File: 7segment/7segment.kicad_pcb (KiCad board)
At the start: 4 copper layers, 22.5 x 25.1 mm, 31 parts, among them J1 AVR-ISP-6, J2 Conn_01x10, J3 Conn_01x02, J4 Conn_01x02, Q1 Q_NPN_BEC, Q2 Q_NPN_BEC, U1 ATmega168PA-AU, U2 HDSP-523

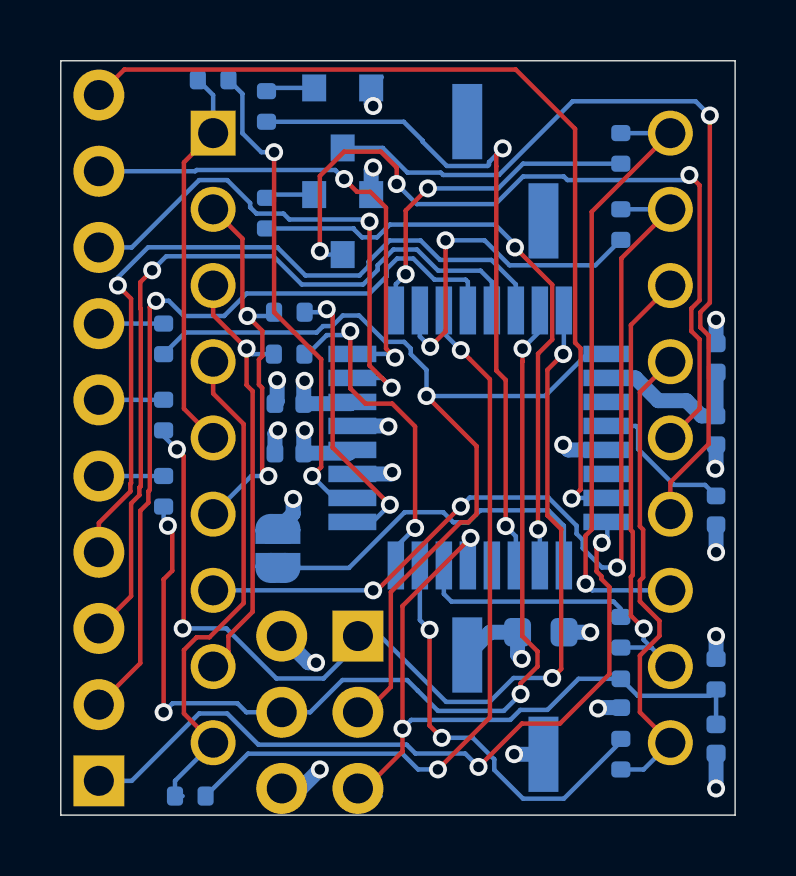
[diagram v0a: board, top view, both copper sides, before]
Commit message: Update 7segment
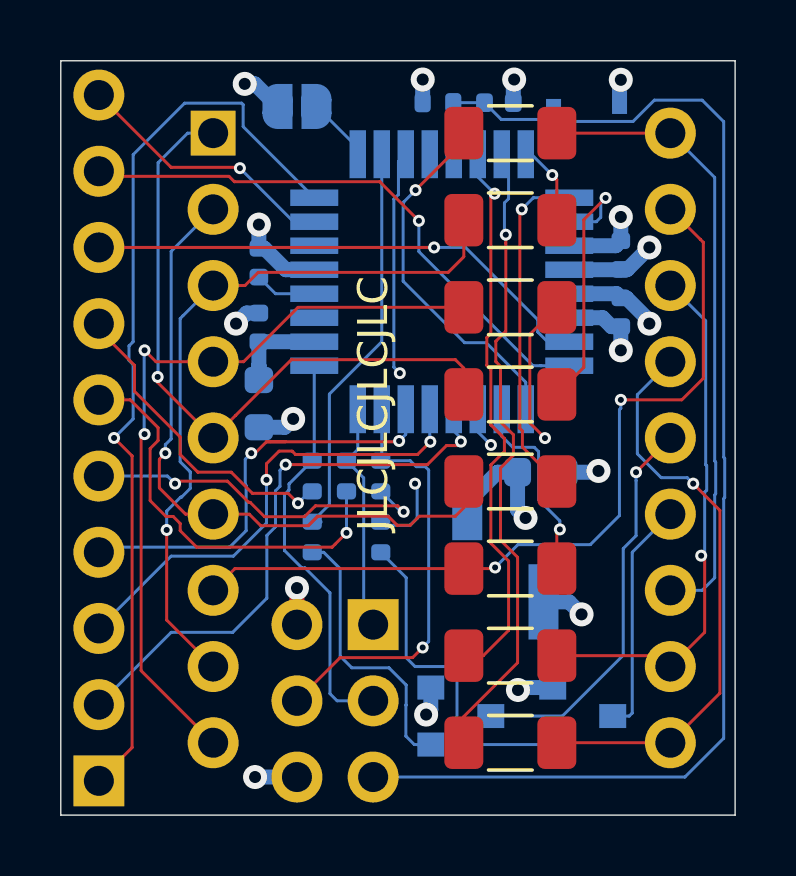
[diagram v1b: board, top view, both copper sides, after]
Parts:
- removed J3: Conn_01x02, Connector_PinHeader_2.54mm:PinHeader_1x02_P2.54mm_Vertical_SMD_Pin1Left
- D1: value D_TVS -> 1N4148; footprint Diode_SMD:D_0402_1005Metric -> Diode_SMD:D_SOD-323F
- L1: footprint Inductor_SMD:L_0402_1005Metric -> Inductor_SMD:L_0603_1608Metric
- R1, R2, R3, R4, R5, R6, R7, R8: footprint Resistor_SMD:R_0402_1005Metric -> Resistor_SMD:R_1206_3216Metric_Pad1.30x1.75mm_HandSolder; moved to F.Cu
- moved D1 21.5 mm to (138.2, 104.5), turned to 180 degrees
- moved Q2 21.5 mm to (138.0, 124.8), turned to 0 degrees
- moved R14 21.2 mm to (133.2, 104.4), turned to 180 degrees
- moved C5 20.1 mm to (135.3, 104.4), turned to 0 degrees
- moved R8 19.5 mm to (135.6, 111.2)
- moved C4 17.3 mm to (127.3, 109.7), turned to 90 degrees
- moved Q1 16.8 mm to (134.0, 124.8), turned to 0 degrees
- moved C2 15.6 mm to (127.3, 111.9), turned to 90 degrees
- moved L1 15.3 mm to (127.3, 114.4), turned to 270 degrees
- moved R13 14.8 mm to (131.3, 118.9), turned to 90 degrees
- moved JP1 14.7 mm to (128.5, 104.5), turned to 180 degrees
- moved R5 14.4 mm to (135.6, 114.1)
- moved C3 12.9 mm to (139.3, 109.5), turned to 90 degrees
- moved R7 12.0 mm to (135.6, 119.9), turned to 0 degrees
- moved C1 11.5 mm to (139.3, 111.4), turned to 90 degrees
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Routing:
- net /MISO: track 34.7 -> 7.70 mm, vias 4 -> 0
- net /ZERO_I_OR_LE: track 30.8 -> 8.93 mm
- net /~RST: track 24.5 -> 44.8 mm, vias 2 -> 0
- net /DIG_2: track 27.9 -> 7.85 mm, vias 1 -> 0
- net /MOSI: track 33.8 -> 14.4 mm, vias 4 -> 1
- net /SCK: track 31.5 -> 13.6 mm, vias 1 -> 0
- net Net-(R8-Pad2): track 25.2 -> 8.21 mm
- net /DIG_1: track 27.1 -> 13.1 mm, vias 3 -> 1
- net Net-(R1-Pad2): track 7.05 -> 18.7 mm, vias 0 -> 1
- net /D4: track 2.16 -> 13.8 mm, vias 0 -> 1
- net /D2: track 25.9 -> 14.8 mm, vias 1 -> 2
- net /D1: track 26.6 -> 16.0 mm, vias 1 -> 2
- net /MODE: track 12.1 -> 2.16 mm
- net /D3: track 2.16 -> 12.1 mm, vias 0 -> 2
- net /DIG_E: track 13.0 -> 22.6 mm, vias 0 -> 1
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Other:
- net class Default: clearance 0.15 -> 0.2; trace_width 0.15 -> 0.1; via_dia 0.6 -> 0.4; via_drill 0.35 -> 0.2
- net class Power added: clearance 0.2, trace_width 0.5, via_dia 0.8, via_drill 0.4
- rule pad_to_mask_clearance: 0 -> 0.0508
- rule trace_clearance: 0.15 -> 0.2
- rule trace_min: 0.15 -> 0.09
- board text added: "5V"
- board text added: "JLCJLCJLCJLC"

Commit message: Update 7 segment
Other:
- net class Default: clearance 0.2 -> 0.127; trace_width 0.1 -> 0.127; via_dia 0.4 -> 0.45
- rule pad_to_mask_clearance: 0.0508 -> 0
- rule trace_clearance: 0.2 -> 0.127
- rule trace_min: 0.09 -> 0.1
- rule via_min_size: 0.4 -> 0.45

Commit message: Update to KiCad 6
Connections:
- net /~RST renamed /~{RST}
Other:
- net class Default removed
- net class Power removed
